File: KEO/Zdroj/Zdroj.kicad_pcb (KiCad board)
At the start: 2 copper layers, 0 parts

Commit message: Téměř celá DPS
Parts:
- added C1: 47uF/63V, Capacitor_THT:CP_Radial_D10.0mm_P5.00mm, F.Cu at (124.3, 109.4)
- added C10: 10uF/63V, Capacitor_THT:CP_Radial_D6.3mm_P2.50mm, F.Cu at (243.9, 67.0)
- added C11: 330pF, Capacitor_THT:C_Disc_D5.0mm_W2.5mm_P5.00mm, F.Cu at (232.3, 79.5)
- added C2: 47uF/63V, Capacitor_THT:CP_Radial_D10.0mm_P5.00mm, F.Cu at (136.7, 109.6)
- added C3: 3300uF/63V, Capacitor_THT:CP_Radial_D22.0mm_P10.00mm_SnapIn, F.Cu at (157.2, 85.3)
- added C4: 4,7uF/35V, Capacitor_THT:CP_Radial_D5.0mm_P2.00mm, F.Cu at (194.4, 87.2)
- added C5: 100uF/16V, Capacitor_THT:CP_Radial_D6.3mm_P2.50mm, F.Cu at (155.5, 117.5)
- added C6: 330pF, Capacitor_THT:C_Disc_D5.0mm_W2.5mm_P5.00mm, F.Cu at (187.0, 114.5)
- added C7: 100N, Capacitor_THT:C_Rect_L7.0mm_W2.5mm_P5.00mm, F.Cu at (230.9, 96.2)
- added C8: 330pF, Capacitor_THT:C_Disc_D5.0mm_W2.5mm_P5.00mm, F.Cu at (202.1, 97.6)
- added C9: 220N, Capacitor_THT:C_Rect_L7.0mm_W2.5mm_P5.00mm, F.Cu at (241.1, 71.8)
- added D1: 1N5402, Diode_THT:D_DO-201AD_P15.24mm_Horizontal, F.Cu at (128.4, 63.0)
- added D10: 5,6V, Diode_THT:D_DO-35_SOD27_P7.62mm_Horizontal, F.Cu at (231.0, 99.4)
- added D11: 1N4448, Diode_THT:D_DO-35_SOD27_P7.62mm_Horizontal, F.Cu at (191.6, 94.4)
- added D12: 3,3V, Diode_THT:D_DO-35_SOD27_P7.62mm_Horizontal, F.Cu at (253.0, 82.7)
- added D13: 1N4001, Diode_THT:D_DO-41_SOD81_P10.16mm_Horizontal, F.Cu at (238.6, 77.8)
- added D14: 1N4448, Diode_THT:D_DO-35_SOD27_P7.62mm_Horizontal, F.Cu at (209.8, 81.5)
- added D2: 1N5402, Diode_THT:D_DO-201AD_P15.24mm_Horizontal, F.Cu at (128.4, 83.2)
- added D3: 1N5402, Diode_THT:D_DO-201AD_P15.24mm_Horizontal, F.Cu at (140.8, 63.0)
- added D4: 1N5402, Diode_THT:D_DO-201AD_P15.24mm_Horizontal, F.Cu at (140.8, 83.0)
- added D5: 1N4448, Diode_THT:D_DO-35_SOD27_P7.62mm_Horizontal, F.Cu at (131.9, 119.6)
- added D6: 1N4448, Diode_THT:D_DO-35_SOD27_P7.62mm_Horizontal, F.Cu at (124.3, 123.8)
- added D7: 33V, Diode_THT:D_DO-35_SOD27_P7.62mm_Horizontal, F.Cu at (188.6, 81.8)
- added D8: LED, LED_THT:LED_D5.0mm, F.Cu at (177.0, 113.7)
- added D9: 5,6V, Diode_THT:D_DO-35_SOD27_P7.62mm_Horizontal, F.Cu at (150.7, 107.6)
- added FID1: Fiducial, Fiducial:Fiducial_0.5mm_Mask1mm, F.Cu at (122.5, 59.0)
- added FID2: Fiducial, Fiducial:Fiducial_0.5mm_Mask1mm, F.Cu at (246.8, 58.5)
- added FID3: Fiducial, Fiducial:Fiducial_0.5mm_Mask1mm, F.Cu at (115.9, 121.7)
- added H1: M3, MountingHole:MountingHole_3.2mm_M3_DIN965_Pad, F.Cu at (115.9, 59.0)
- added H2: M3, MountingHole:MountingHole_3.2mm_M3_DIN965_Pad, F.Cu at (253.0, 58.7)
- added H3: M3, MountingHole:MountingHole_3.2mm_M3_DIN965_Pad, F.Cu at (116.0, 128.7)
- added H4: M3, MountingHole:MountingHole_3.2mm_M3_DIN965_Pad, F.Cu at (253.0, 128.7)
- added J1: 24V AC, TerminalBlock_Phoenix:TerminalBlock_Phoenix_MKDS-3-2-5.08_1x02_P5.08mm_Horizontal, F.Cu at (119.0, 78.5)
- added J2: OUT, TerminalBlock_Phoenix:TerminalBlock_Phoenix_MKDS-3-2-5.08_1x02_P5.08mm_Horizontal, F.Cu at (236.4, 63.0)
- added J3: Q7, TerminalBlock_Phoenix:TerminalBlock_Phoenix_MKDS-1,5-3-5.08_1x03_P5.08mm_Horizontal, F.Cu at (210.9, 62.9)
- added Q1: BC547, Package_TO_SOT_THT:TO-92_Inline, F.Cu at (182.8, 75.3)
- added Q2: BC547, Package_TO_SOT_THT:TO-92_Inline, F.Cu at (182.8, 84.5)
- added Q3: BC557, Package_TO_SOT_THT:TO-92_Inline, F.Cu at (183.6, 93.5)
- added Q4: BC557, Package_TO_SOT_THT:TO-92_Inline, F.Cu at (146.2, 120.0)
- added Q5: BC547, Package_TO_SOT_THT:TO-92_Inline, F.Cu at (250.7, 86.5)
- added Q6: BD139, Package_TO_SOT_THT:TO-126-3_Vertical, F.Cu at (214.4, 75.0)
- added R1: 82R, Resistor_THT:R_Axial_DIN0207_L6.3mm_D2.5mm_P7.62mm_Horizontal, F.Cu at (134.4, 94.8)
- added R11: 2,2K, Resistor_THT:R_Axial_DIN0207_L6.3mm_D2.5mm_P7.62mm_Horizontal, F.Cu at (226.6, 104.6)
- added R12: 10K, Resistor_THT:R_Axial_DIN0207_L6.3mm_D2.5mm_P7.62mm_Horizontal, F.Cu at (217.8, 104.6)
- added R13: 6,8K, Resistor_THT:R_Axial_DIN0207_L6.3mm_D2.5mm_P7.62mm_Horizontal, F.Cu at (217.8, 115.0)
- added R14: 18K, Resistor_THT:R_Axial_DIN0207_L6.3mm_D2.5mm_P7.62mm_Horizontal, F.Cu at (235.4, 104.6)
- added R15: 2,2K, Resistor_THT:R_Axial_DIN0207_L6.3mm_D2.5mm_P7.62mm_Horizontal, F.Cu at (223.3, 89.3)
- added R16: 18K, Resistor_THT:R_Axial_DIN0207_L6.3mm_D2.5mm_P7.62mm_Horizontal, F.Cu at (238.9, 90.2)
- added R17: 18K, Resistor_THT:R_Axial_DIN0207_L6.3mm_D2.5mm_P7.62mm_Horizontal, F.Cu at (241.2, 82.6)
- added R18: 0,47R, Resistor_THT:R_Axial_Power_L25.0mm_W6.4mm_P30.48mm, F.Cu at (245.0, 128.8)
- added R19: 1K, Resistor_THT:R_Axial_DIN0207_L6.3mm_D2.5mm_P7.62mm_Horizontal, F.Cu at (215.8, 85.4)
- added R2: 2,2K, Resistor_THT:R_Axial_DIN0414_L11.9mm_D4.5mm_P15.24mm_Horizontal, F.Cu at (172.0, 75.0)
- added R20: 1K, Resistor_THT:R_Axial_DIN0207_L6.3mm_D2.5mm_P7.62mm_Horizontal, F.Cu at (220.9, 70.6)
- added R21: 47K, Resistor_THT:R_Axial_DIN0207_L6.3mm_D2.5mm_P7.62mm_Horizontal, F.Cu at (227.3, 84.4)
- added R22: 2,2K, Resistor_THT:R_Axial_DIN0207_L6.3mm_D2.5mm_P7.62mm_Horizontal, F.Cu at (205.5, 99.0)
- added R23: 2,2K, Resistor_THT:R_Axial_DIN0207_L6.3mm_D2.5mm_P7.62mm_Horizontal, F.Cu at (216.7, 99.0)
- added R3: 2,2K, Resistor_THT:R_Axial_DIN0207_L6.3mm_D2.5mm_P7.62mm_Horizontal, F.Cu at (177.6, 82.6)
- added R4: 2,2K, Resistor_THT:R_Axial_DIN0207_L6.3mm_D2.5mm_P7.62mm_Horizontal, F.Cu at (174.4, 100.4)
- added R5: 2,2K, Resistor_THT:R_Axial_DIN0207_L6.3mm_D2.5mm_P7.62mm_Horizontal, F.Cu at (146.3, 115.2)
- added R6: 2,2K, Resistor_THT:R_Axial_DIN0207_L6.3mm_D2.5mm_P7.62mm_Horizontal, F.Cu at (177.6, 86.4)
- added R7: 10K, Resistor_THT:R_Axial_DIN0207_L6.3mm_D2.5mm_P7.62mm_Horizontal, F.Cu at (179.0, 100.4)
- added R8: 10K, Resistor_THT:R_Axial_DIN0207_L6.3mm_D2.5mm_P7.62mm_Horizontal, F.Cu at (170.2, 116.4)
- added R9: 56K, Resistor_THT:R_Axial_DIN0207_L6.3mm_D2.5mm_P7.62mm_Horizontal, F.Cu at (222.2, 104.6)
- added RV1: 10K, Potentiometer_THT:Potentiometer_Piher_PC-16_Single_Horizontal, F.Cu at (177.0, 118.8)
- added RV2: 10K, Potentiometer_THT:Potentiometer_Piher_PC-16_Single_Horizontal, F.Cu at (222.2, 118.8)
- added RV3: 220R, Potentiometer_THT:Potentiometer_Piher_PT-6-V_Vertical, F.Cu at (165.9, 118.7)
- added U1: TL082, Package_DIP:DIP-8_W7.62mm, F.Cu at (193.0, 112.2)
- added U2: TL082, Package_DIP:DIP-8_W7.62mm, F.Cu at (205.6, 112.2)
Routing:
- net GND: track 0.00 -> 340.7 mm
- net /C_Q7: track 0.00 -> 184.7 mm
- net Net-(D13-A): track 0.00 -> 183.0 mm
- net Net-(D12-A): track 0.00 -> 165.0 mm
- net /U1,U2+: track 0.00 -> 112.1 mm
- net /E_Q7: track 0.00 -> 67.0 mm
- net Net-(U1B--): track 0.00 -> 61.3 mm
- net Net-(C8-Pad2): track 0.00 -> 60.8 mm
- net Net-(D10-K): track 0.00 -> 54.2 mm
- net Net-(D6-A): track 0.00 -> 41.6 mm
- net Net-(D3-A): track 0.00 -> 40.7 mm
- net Net-(R9-Pad2): track 0.00 -> 38.1 mm
- net Net-(D11-A): track 0.00 -> 36.9 mm
- net Net-(D11-K): track 0.00 -> 33.6 mm
- net Net-(D10-A): track 0.00 -> 27.4 mm
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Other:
- board outline added: 146 x 79 mm

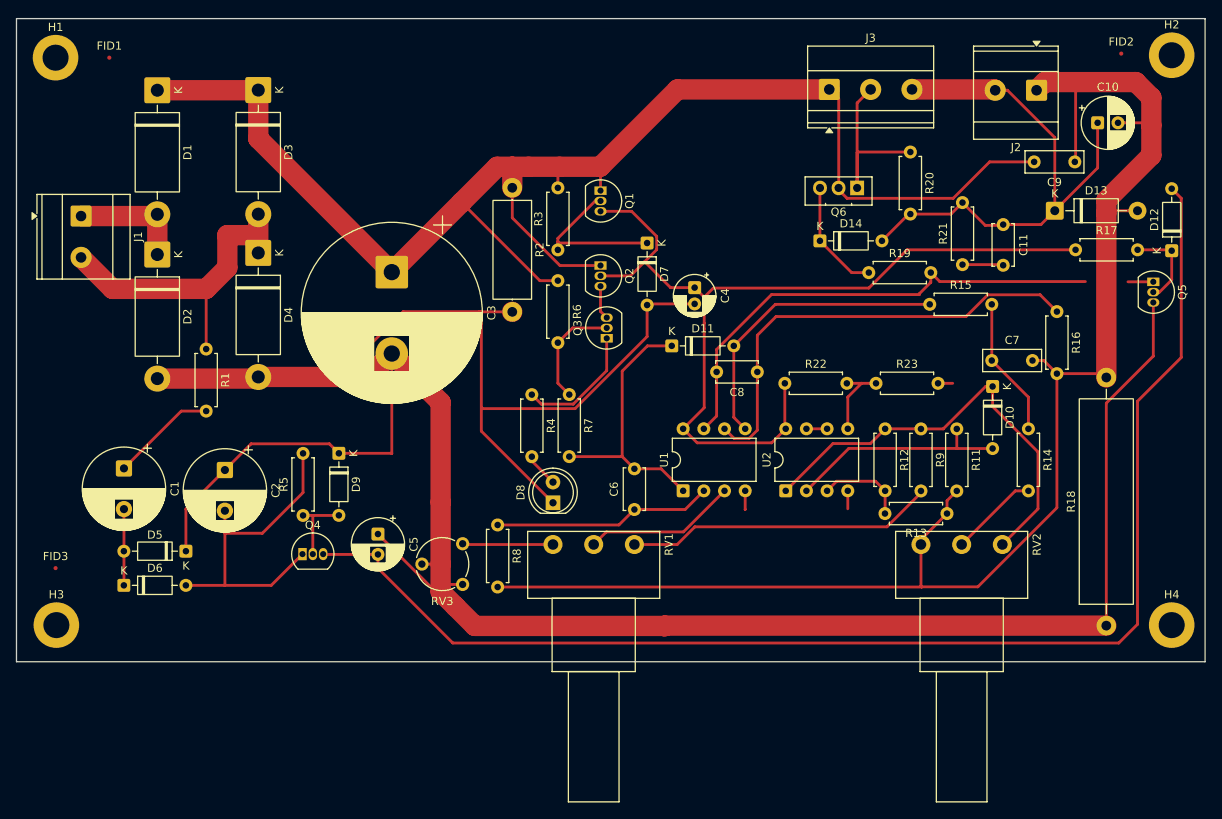
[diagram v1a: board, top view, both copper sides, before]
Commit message: Author text on PCB
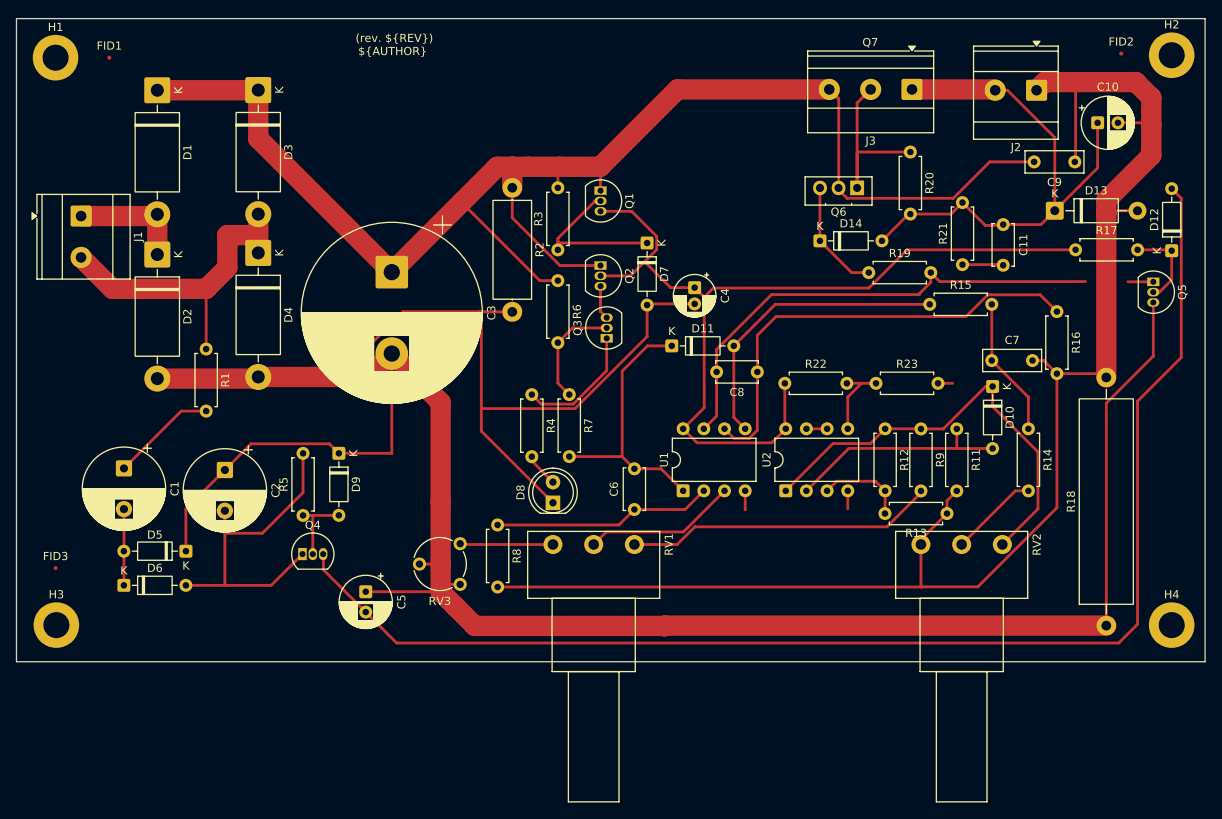
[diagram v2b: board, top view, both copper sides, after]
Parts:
- moved J3 10.2 mm to (221.1, 62.9), turned to 180 degrees
- moved C5 7.24 mm to (154.0, 124.6)
- moved RV3 0.30 mm to (165.6, 118.7)
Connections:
- J3 pad 1: /C_Q7 -> /E_Q7
- J3 pad 3: /E_Q7 -> /C_Q7
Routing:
- net GND: track 340.7 -> 339.3 mm
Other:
- board text added: "${TITLE} (rev. ${REV}) ${AUTHOR}"
- board text added: "Q7"

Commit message: KEO GND
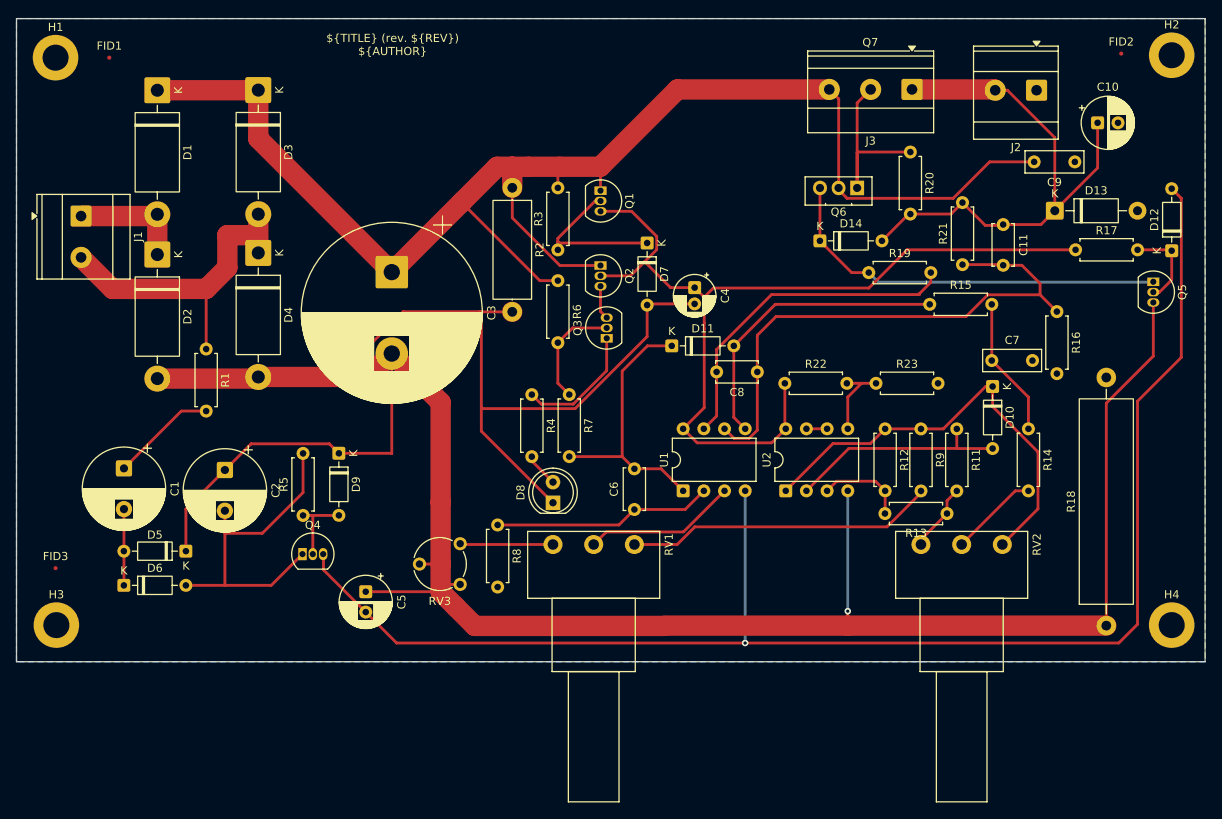
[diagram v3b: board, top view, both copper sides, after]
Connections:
- C10 pad 2: Net-(D13-A) -> GND
- C2 pad 1: GND -> Net-(D2-A)
- C3 pad 2: GND -> Net-(D2-A)
- C4 pad 2: GND -> Net-(D2-A)
- C5 pad 1: GND -> Net-(D2-A)
- C7 pad 2: Net-(D13-A) -> GND
- C9 pad 1: Net-(D13-A) -> GND
- D13 pad 2: Net-(D13-A) -> GND
- D2 pad 2: GND -> Net-(D2-A)
- D4 pad 2: GND -> Net-(D2-A)
- D5 pad 1: GND -> Net-(D2-A)
- D7 pad 2: GND -> Net-(D2-A)
- D8 pad 1: GND -> Net-(D2-A)
- D9 pad 1: GND -> Net-(D2-A)
- J2 pad 1: Net-(D13-A) -> GND
- Q5 pad 3: GND -> Net-(D2-A)
- R11 pad 2: Net-(D13-A) -> GND
- R13 pad 2: Net-(D13-A) -> GND
- R16 pad 2: Net-(D13-A) -> GND
- R18 pad 1: GND -> Net-(D2-A)
- R18 pad 2: Net-(D13-A) -> GND
- R2 pad 2: GND -> Net-(D2-A)
- R8 pad 2: Net-(D13-A) -> GND
- RV2 pad 1: Net-(D13-A) -> GND
- RV3 pad 2: GND -> Net-(D2-A)
- RV3 pad 3: GND -> Net-(D2-A)
- U2 pad 4: GND -> Net-(D2-A)
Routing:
- net Net-(D2-A): track 0.00 -> 351.7 mm, vias 0 -> 1
- net GND: track 339.3 -> 9.45 mm
- net Net-(D13-A): track 183.0 -> 0.00 mm
- net Net-(D14-K): track 17.2 -> 49.6 mm
- net Net-(C8-Pad2): track 60.8 -> 41.4 mm
- net Net-(D12-A): track 165.1 -> 181.5 mm, vias 0 -> 1
- net Net-(U1B--): track 61.3 -> 68.2 mm
- added copper zone on B.Cu, net GND

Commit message: KEO Drobné úpravy
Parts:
- removed FID3: Fiducial, Fiducial:Fiducial_0.5mm_Mask1mm
- moved FID2 63.9 mm to (253.1, 122.1)
- moved FID1 0.21 mm to (122.3, 59.0)
- moved H2 0.18 mm to (252.9, 58.9)
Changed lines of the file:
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@@
 		(allow_soldermask_bridges_in_footprints no)
 		(tenting front back)
+		(aux_axis_origin 111.1 133.2)
+		(grid_origin 111.1 133.2)
 		(pcbplotparams
 			(layerselection 0x00000000_00000000_55555555_5755f5ff)
@@
 	(footprint "Fiducial:Fiducial_0.5mm_Mask1mm"
 		(layer "F.Cu")
-		(at 246.8 58.5)
+		(at 253.1 122.1)
 		(descr "Fiducial, circular marking, 0.5mm bare copper, 1mm soldermask opening (Level C)")
 		(tags "fiducial")
@@
 	(footprint "MountingHole:MountingHole_3.2mm_M3_DIN965_Pad"
 		(layer "F.Cu")
-		(at 253 58.7)
+		(at 252.938193 58.869096)
 		(descr "Mounting Hole 3.2mm, M3, generated by kicad-footprint-generator mountinghole.py")
 		(tags "mountinghole M3 DIN965")
@@
 		(tags "Resistor Axial_DIN0207 series Axial Horizontal pin pitch 7.62mm 0.25W = 1/4W length 6.3mm diameter 2.5mm")
 		(property "Reference" "R13"
-			(at 3.82 2.4 0)
+			(at -2.68 0 0)
 			(layer "F.SilkS")
 			(effects
@@
 		(tags "to-92 sc-43 sc-43a sot54 PA33 transistor")
 		(property "Reference" "Q4"
-			(at 1.27 -3.56 0)
+			(at 5.07 -0.077621 0)
 			(layer "F.SilkS")
 			(effects
@@
 		(tags "Resistor Axial_DIN0207 series Axial Horizontal pin pitch 7.62mm 0.25W = 1/4W length 6.3mm diameter 2.5mm")
 		(property "Reference" "R5"
-			(at 3.81 -2.37 90)
+			(at 4.827621 -2.2 90)
 			(layer "F.SilkS")
 			(effects
@@
 	(footprint "Fiducial:Fiducial_0.5mm_Mask1mm"
 		(layer "F.Cu")
-		(at 122.5 59)
+		(at 122.290518 58.961447)
 		(descr "Fiducial, circular marking, 0.5mm bare copper, 1mm soldermask opening (Level C)")
 		(tags "fiducial")
@@
 		)
 	)
-	(footprint "Fiducial:Fiducial_0.5mm_Mask1mm"
-		(layer "F.Cu")
-		(at 115.9 121.7)
-		(descr "Fiducial, circular marking, 0.5mm bare copper, 1mm soldermask opening (Level C)")
-		(tags "fiducial")
-		(property "Reference" "FID3"
-			(at 0 -1.45 0)
-			(layer "F.SilkS")
-			(effects
-				(font
-					(size 1 1)
-					(thickness 0.15)
-				)
-			)
-		)
-		(property "Value" "Fiducial"
-			(at 0 1.45 0)
-			(layer "F.Fab")
-			(effects
-				(font
-					(size 1 1)
-					(thickness 0.15)
-				)
-			)
-		)
-		(property "Datasheet" "~"
-			(at 0 0 0)
-			(layer "F.Fab")
-			(hide yes)
-			(effects
-				(font
-					(size 1.27 1.27)
-					(thickness 0.15)
-				)
-			)
-		)
-		(property "Description" "Fiducial Marker"
-			(at 0 0 0)
-			(layer "F.Fab")
-			(hide yes)
-			(effects
-				(font
-					(size 1.27 1.27)
-					(thickness 0.15)
-				)
-			)
-		)
-		(property ki_fp_filters "Fiducial*")
-		(sheetname "/")
-		(sheetfile "Zdroj.kicad_sch")
-		(attr smd exclude_from_bom)
-		(fp_circle
-			(center 0 0)
-			(end 0.75 0)
-			(stroke
-				(width 0.05)
-				(type solid)
-			)
-			(fill no)
-			(layer "F.CrtYd")
-		)
-		(fp_circle
-			(center 0 0)
-			(end 0.5 0)
-			(stroke
-				(width 0.1)
-				(type solid)
-			)
-			(fill no)
-			(layer "F.Fab")
-		)
-		(fp_text user "${REFERENCE}"
-			(at 0 0 0)
-			(layer "F.Fab")
-			(effects
-				(font
-					(size 0.25 0.25)
-					(thickness 0.04)
-				)
-			)
-		)
-		(pad "" smd circle
-			(at 0 0)
-			(size 0.5 0.5)
-			(layers "F.Cu" "F.Mask")
-			(solder_mask_margin 0.25)
-			(clearance 0.35)
-		)
-		(embedded_fonts no)
-	)
 	(gr_rect
 		(start 111.1 54.2)
@@
 	)
 	(segment
-		(start 163.275 113.675)
-		(end 163.2 113.6)
-		(width 0.35)
-		(layer "F.Cu")
-		(net 10)
-	)
-	(segment
 		(start 158.6 90.2)
 		(end 154.6 94.2)
@@
 	)
 	(segment
-		(start 134.2 87.6)
-		(end 134.4 87.4)
-		(width 0.35)
-		(layer "F.Cu")
-		(net 15)
-	)
-	(segment
